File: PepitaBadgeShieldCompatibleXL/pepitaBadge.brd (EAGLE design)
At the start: 92.9 x 65 mm, 27 parts, among them IC2 REG1117, U1 AVR328P

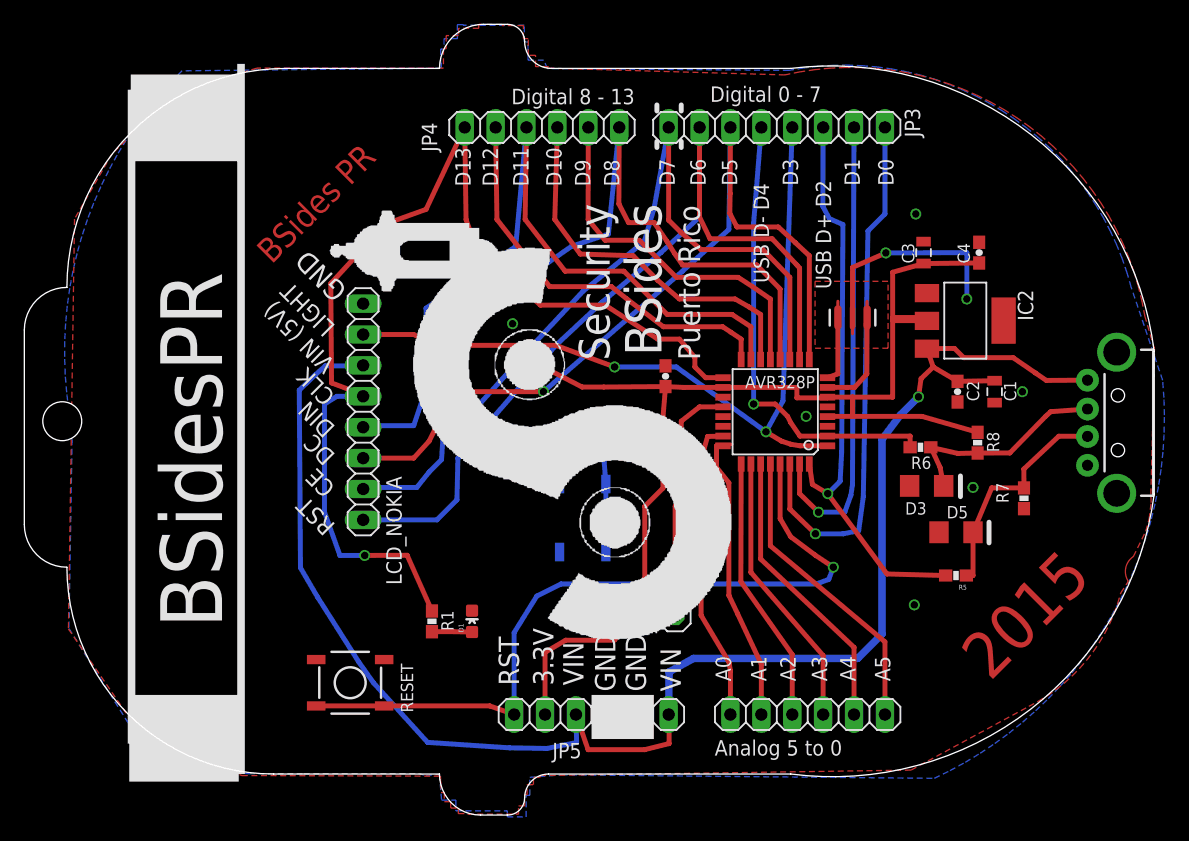
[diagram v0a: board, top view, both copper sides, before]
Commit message: Smooth PCB border and adding some Arduino code
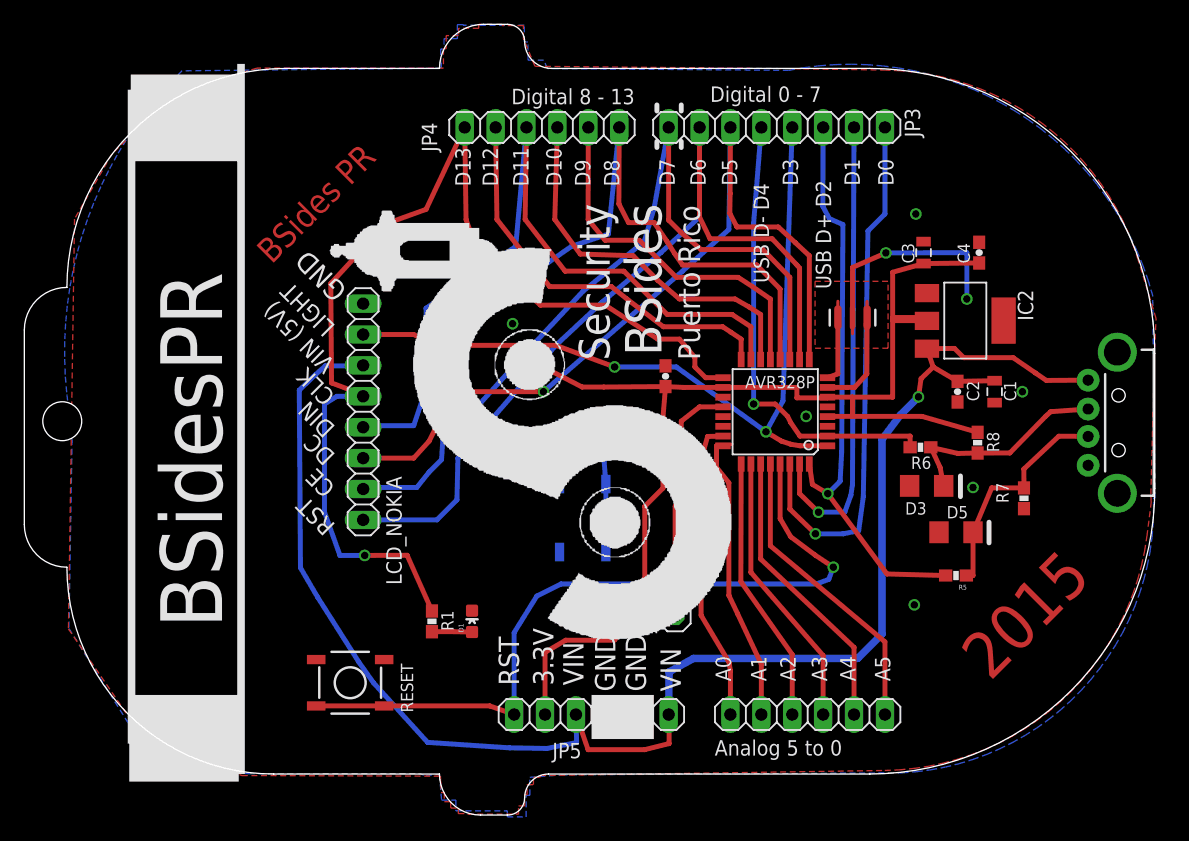
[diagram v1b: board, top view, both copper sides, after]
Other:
- outline, holes or cut-outs redrawn

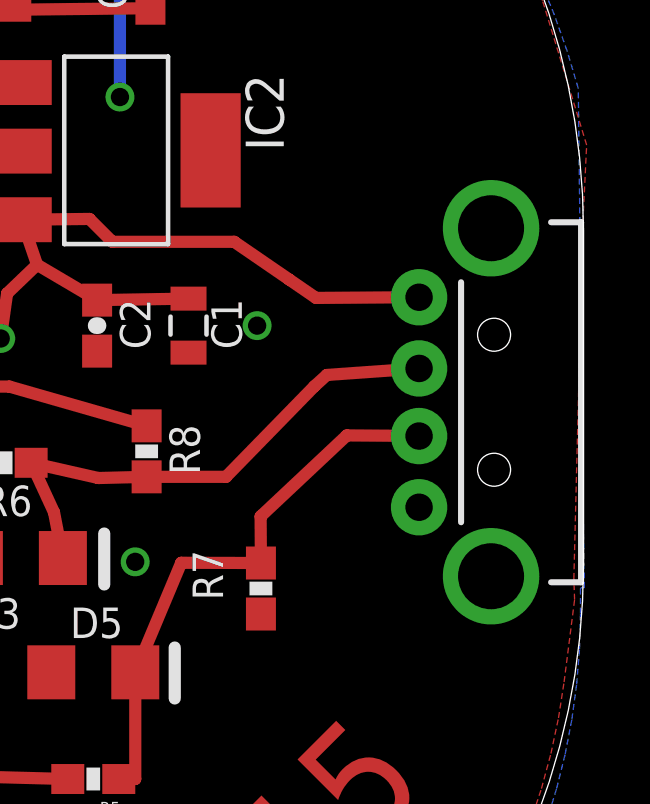
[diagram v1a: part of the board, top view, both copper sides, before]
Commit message: Trying to make this work, as of now first sent to manufacturing did not work with 6mills paths. changed to 10 mills.
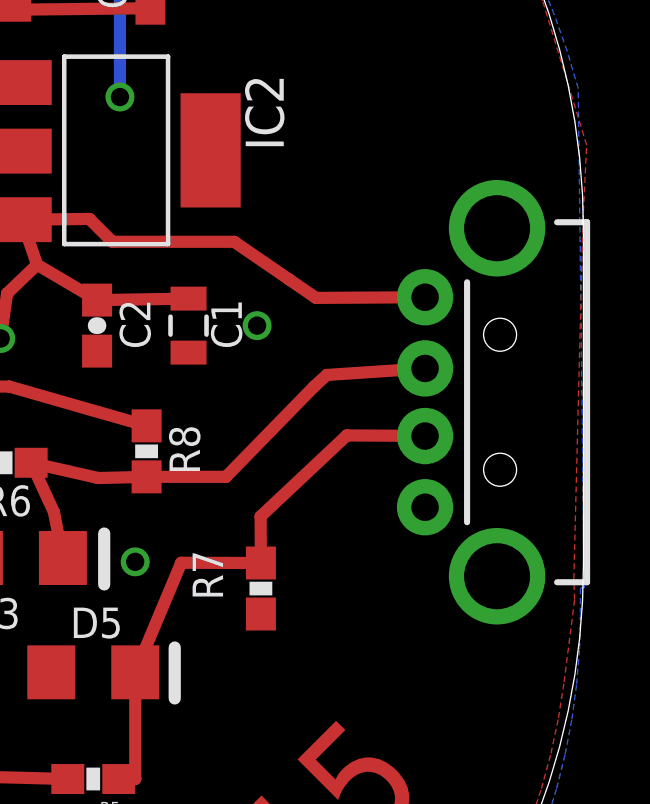
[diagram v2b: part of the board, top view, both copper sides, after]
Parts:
- moved JP1 0.20 mm to (89.9, 29.2)
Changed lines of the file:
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@@
 <attribute name="VALUE" x="53.192" y="33.227" size="0.4064" layer="27" font="vector" rot="R180"/>
 </element>
-<element name="JP1" library="SparkFun-Connectors" package="USB-A-H" value="USB-A-H" x="89.72" y="29.25" smashed="yes" rot="R180">
-<attribute name="PROD_ID" value="CONN-08367" x="89.72" y="29.25" size="1.778" layer="27" rot="R180" display="off"/>
+<element name="JP1" library="SparkFun-Connectors" package="USB-A-H" value="USB-A-H" x="89.92" y="29.25" smashed="yes" rot="R180">
+<attribute name="PROD_ID" value="CONN-08367" x="89.92" y="29.25" size="1.778" layer="27" rot="R180" display="off"/>
 </element>
 <element name="IC2" library="burr-brown" package="SOT223" value="REG1117" x="77.222" y="37.646" rot="R270">
@@
 <contactref element="D3" pad="2"/>
 <contactref element="JP1" pad="D-"/>
-<wire x1="87.32" y1="30.377" x2="84.2455" y2="30.159" width="0.4064" layer="1"/>
+<wire x1="87.52" y1="30.377" x2="84.2455" y2="30.159" width="0.4064" layer="1"/>
 <wire x1="84.2455" y1="30.159" x2="83.829" y2="29.7805" width="0.4064" layer="1"/>
 <wire x1="83.829" y1="29.7805" x2="80.884" y2="26.7635" width="0.4064" layer="1"/>
@@
 <contactref element="D5" pad="2"/>
 <contactref element="JP1" pad="D+"/>
-<wire x1="87.32" y1="28.123" x2="86.995" y2="28.131" width="0.4064" layer="1"/>
+<wire x1="87.52" y1="28.123" x2="86.995" y2="28.131" width="0.4064" layer="1"/>
 <wire x1="86.995" y1="28.131" x2="84.9115" y2="28.1435" width="0.4064" layer="1"/>
 <wire x1="84.9115" y1="28.1435" x2="82.0375" y2="25.444" width="0.4064" layer="1"/>
@@
 <contactref element="C2" pad="1"/>
 <wire x1="79.635" y1="32.704" x2="76.587" y2="32.654" width="0.4064" layer="1"/>
-<wire x1="87.32" y1="32.75" x2="83.883" y2="32.7276" width="0.4064" layer="1"/>
+<wire x1="87.52" y1="32.75" x2="83.883" y2="32.7276" width="0.4064" layer="1"/>
 <wire x1="83.883" y1="32.7276" x2="82.9919" y2="33.3401" width="0.4064" layer="1"/>
 <wire x1="82.9919" y1="33.3401" x2="81.159" y2="34.598" width="0.4064" layer="1"/>
